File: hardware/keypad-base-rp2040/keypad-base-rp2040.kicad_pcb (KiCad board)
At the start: 2 copper layers, 150.2 x 64.2 mm, 66 parts, among them CON1 AVR-ISP-6, J1 USB_C_Receptacle_USB2.0, J2 Conn_01x02, J3 Conn_01x02, Q1 AO3400A, SW1 Switch_SW_Push, SW2 Switch_SW_Push, SW3 Switch_SW_Push, SW4 Switch_SW_Push, SW5 Switch_SW_Push, SW6 Switch_SW_Push, SW7 Switch_SW_Push, SW8 Switch_SW_Push, U1 ATmega32U4-MU, U10 AP2112K-3.3, U11 W25Q128JVS, U3 IE096HQ1301CL, U4 IE096HQ1301CL, U5 IE096HQ1301CL, U6 IE096HQ1301CL, U7 IE096HQ1301CL, U8 IE096HQ1301CL, X1 16MHz

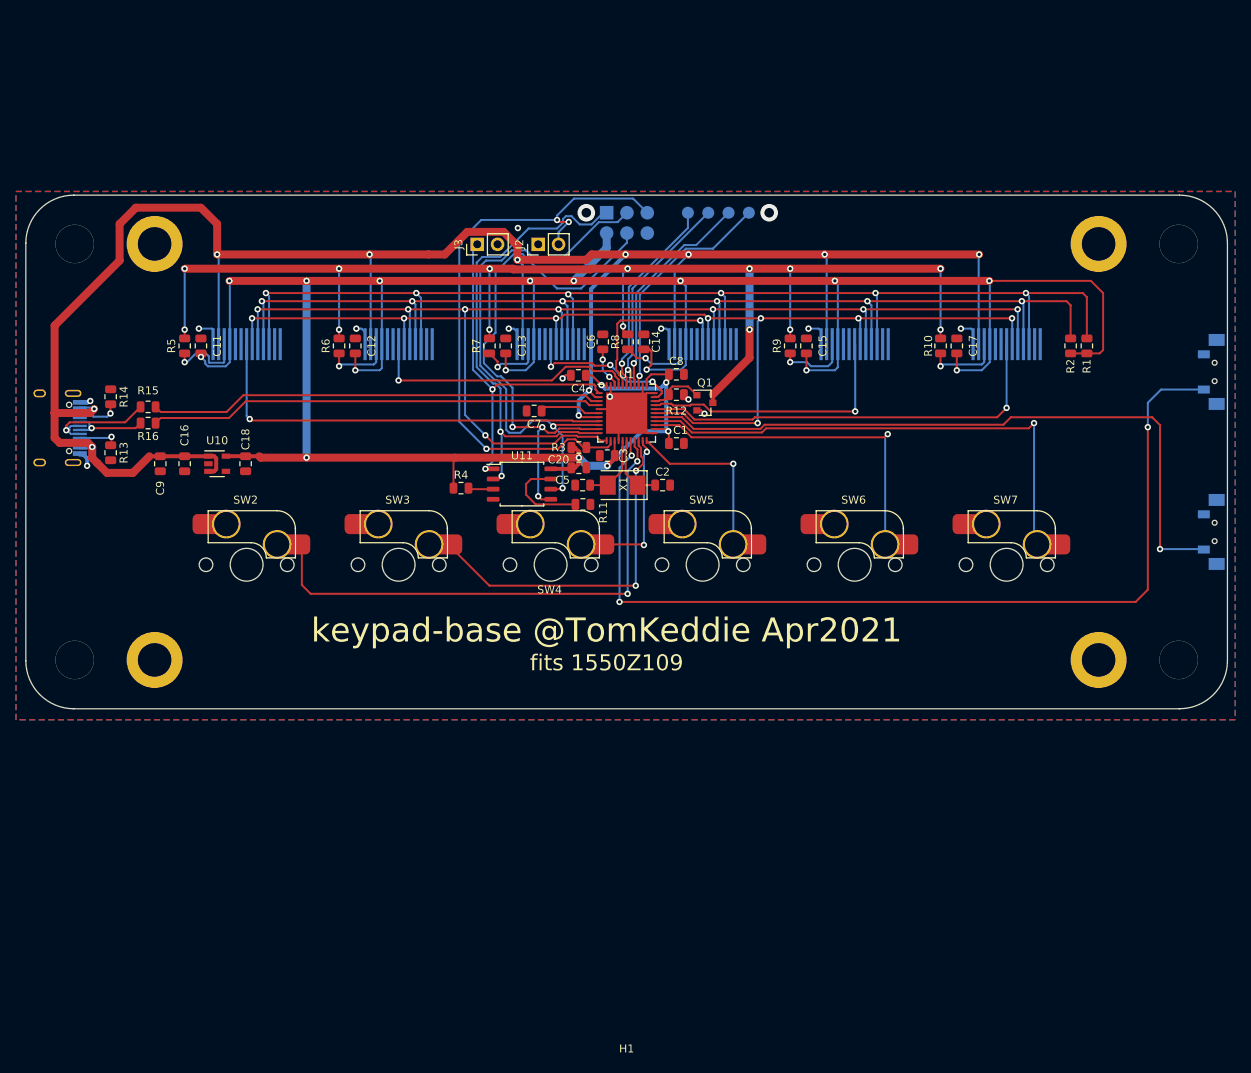
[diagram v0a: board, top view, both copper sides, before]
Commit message: hardware/keypad-base-rp2040: update to latest kicad file format
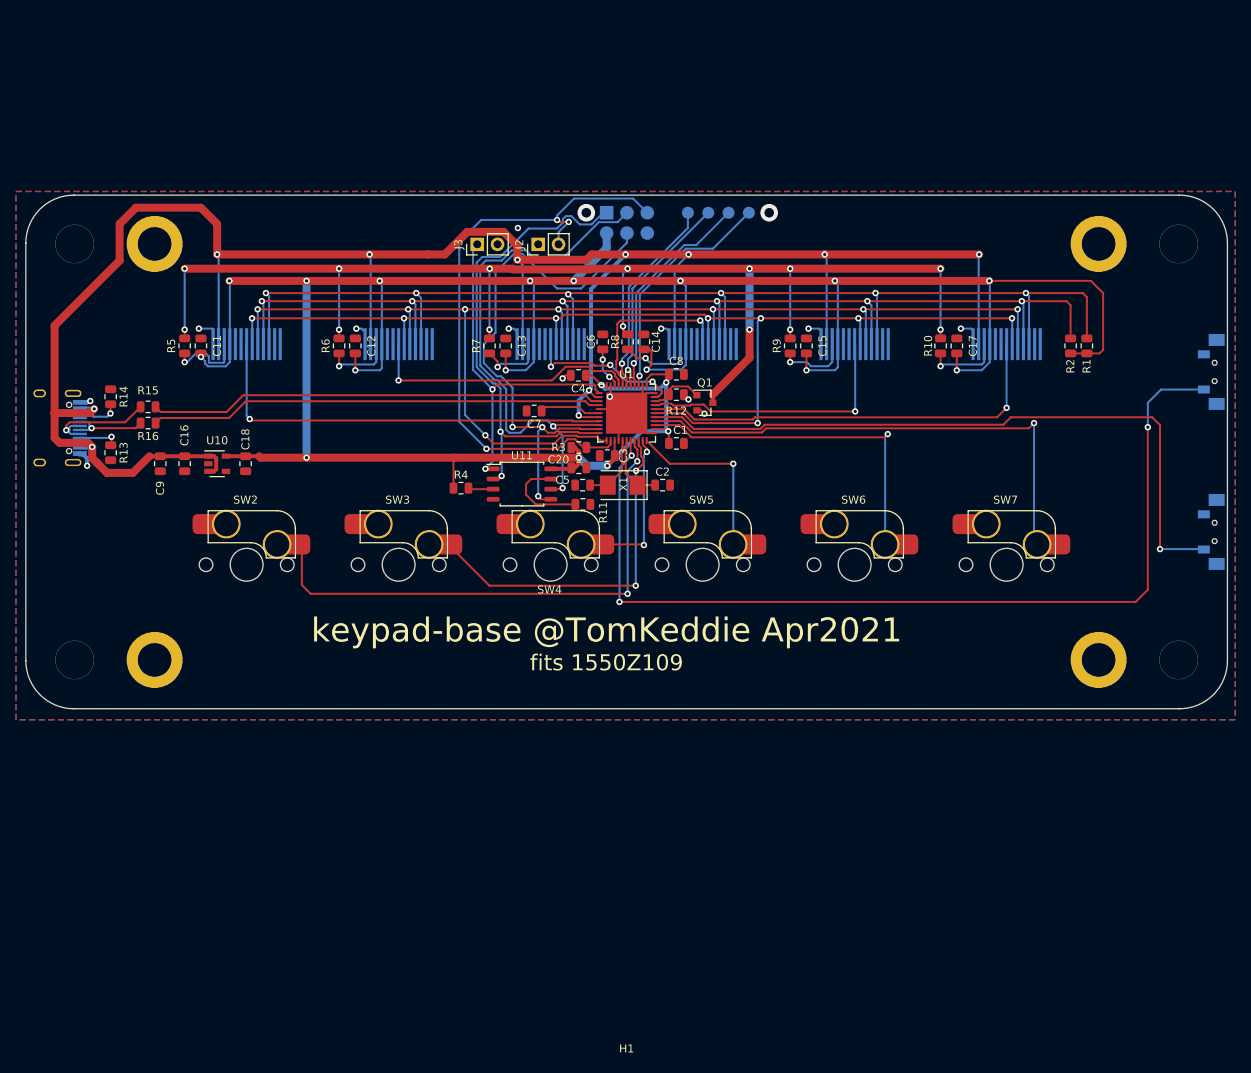
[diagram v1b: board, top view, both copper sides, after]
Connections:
- net /~CS2 renamed /~{CS2}
- net /~CS3 renamed /~{CS3}
- net /~CS4 renamed /~{CS4}
- net /~CS5 renamed /~{CS5}
- net /~CS6 renamed /~{CS6}
- net /~CS7 renamed /~{CS7}
- net /~FLASH_CS renamed /~{FLASH_CS}
- net /~LCDRESET renamed /~{LCDRESET}
- net /~RESET renamed /~{RESET}
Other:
- net class Default removed

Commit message: hardware/keypad0base-rp2040: first pass at rp2040 based design
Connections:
- U1 pad 29: /~{CS7} -> /~{CS6}
- U1 pad 30: /~{CS6} -> /~{CS5}
- U1 pad 32: /~{CS5} -> /~{CS4}
- U1 pad 40: /~{CS4} -> /~{CS3}
- U1 pad 41: /~{CS3} -> /~{CS2}
- U1 pad 8: /~{CS2} -> /~{CS1}
- U3 pad 7: /~{CS2} -> /~{CS1}
- U4 pad 7: /~{CS3} -> /~{CS2}
- U5 pad 7: /~{CS5} -> /~{CS4}
- U6 pad 7: /~{CS4} -> /~{CS3}
- U7 pad 7: /~{CS6} -> /~{CS5}
- U8 pad 7: /~{CS7} -> /~{CS6}
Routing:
- net /~{CS1}: track 0.00 -> 53.3 mm, vias 0 -> 1
- net /~{CS7}: track 53.2 -> 0.00 mm, vias 1 -> 0
- net /~{CS6}: track 34.1 -> 53.2 mm
- net /~{CS2}: track 53.3 -> 34.3 mm
- net /~{CS5}: track 19.8 -> 34.1 mm, vias 3 -> 1
- net /~{CS3}: track 34.3 -> 21.7 mm
- net /~{CS4}: track 21.7 -> 19.8 mm, vias 1 -> 3
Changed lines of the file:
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@@
   (net 36 "Net-(U3-Pad1)")
   (net 37 "Net-(U3-Pad2)")
-  (net 38 "/~{CS2}")
+  (net 38 "/~{CS1}")
   (net 39 "Net-(U4-Pad1)")
   (net 40 "Net-(U4-Pad2)")
-  (net 41 "/~{CS3}")
+  (net 41 "/~{CS2}")
   (net 42 "Net-(U5-Pad1)")
   (net 43 "Net-(U5-Pad2)")
-  (net 44 "/~{CS5}")
+  (net 44 "/~{CS4}")
   (net 45 "Net-(U6-Pad1)")
   (net 46 "Net-(U6-Pad2)")
-  (net 47 "/~{CS4}")
+  (net 47 "/~{CS3}")
   (net 48 "Net-(U7-Pad1)")
   (net 49 "Net-(U7-Pad2)")
-  (net 50 "/~{CS6}")
+  (net 50 "/~{CS5}")
   (net 51 "Net-(U8-Pad1)")
   (net 52 "Net-(U8-Pad2)")
-  (net 53 "/~{CS7}")
+  (net 53 "/~{CS6}")
   (net 54 "/USB_N")
   (net 55 "/USB_P")
@@
       (net 24 "+5V"))
     (pad "8" smd roundrect locked (at -3.4375 1) (size 0.875 0.25) (layers "F.Cu" "F.Paste" "F.Mask") (roundrect_rratio 0.25)
-      (net 38 "/~{CS2}"))
+      (net 38 "/~{CS1}"))
     (pad "9" smd roundrect locked (at -3.4375 1.5) (size 0.875 0.25) (layers "F.Cu" "F.Paste" "F.Mask") (roundrect_rratio 0.25)
       (net 8 "/SCK"))
@@
       (net 26 "/~{LCDRESET}"))
     (pad "29" smd roundrect locked (at 3.4375 -0.5) (size 0.875 0.25) (layers "F.Cu" "F.Paste" "F.Mask") (roundrect_rratio 0.25)
-      (net 53 "/~{CS7}"))
+      (net 53 "/~{CS6}"))
     (pad "30" smd roundrect locked (at 3.4375 -1) (size 0.875 0.25) (layers "F.Cu" "F.Paste" "F.Mask") (roundrect_rratio 0.25)
-      (net 50 "/~{CS6}"))
+      (net 50 "/~{CS5}"))
     (pad "31" smd roundrect locked (at 3.4375 -1.5) (size 0.875 0.25) (layers "F.Cu" "F.Paste" "F.Mask") (roundrect_rratio 0.25)
       (net 29 "/BACKLIGHT"))
     (pad "32" smd roundrect locked (at 3.4375 -2) (size 0.875 0.25) (layers "F.Cu" "F.Paste" "F.Mask") (roundrect_rratio 0.25)
-      (net 44 "/~{CS5}"))
+      (net 44 "/~{CS4}"))
     (pad "33" smd roundrect locked (at 3.4375 -2.5) (size 0.875 0.25) (layers "F.Cu" "F.Paste" "F.Mask") (roundrect_rratio 0.25)
       (net 1 "GND"))
@@
       (net 20 "/TCK"))
     (pad "40" smd roundrect locked (at -0.5 -3.4375) (size 0.25 0.875) (layers "F.Cu" "F.Paste" "F.Mask") (roundrect_rratio 0.25)
-      (net 47 "/~{CS4}"))
+      (net 47 "/~{CS3}"))
     (pad "41" smd roundrect locked (at -1 -3.4375) (size 0.25 0.875) (layers "F.Cu" "F.Paste" "F.Mask") (roundrect_rratio 0.25)
-      (net 41 "/~{CS3}"))
+      (net 41 "/~{CS2}"))
     (pad "42" smd roundrect locked (at -1.5 -3.4375) (size 0.25 0.875) (layers "F.Cu" "F.Paste" "F.Mask") (roundrect_rratio 0.25)
       (net 5 "/AREF"))
@@
       (net 26 "/~{LCDRESET}"))
     (pad "7" smd rect locked (at 0 0 180) (size 0.4 4) (layers "B.Cu" "B.Paste" "B.Mask")
-      (net 38 "/~{CS2}"))
+      (net 38 "/~{CS1}"))
     (pad "8" smd rect locked (at 0.7 0 180) (size 0.4 4) (layers "B.Cu" "B.Paste" "B.Mask")
       (net 1 "GND"))
@@
       (net 26 "/~{LCDRESET}"))
     (pad "7" smd rect locked (at 0 0 180) (size 0.4 4) (layers "B.Cu" "B.Paste" "B.Mask")
-      (net 41 "/~{CS3}"))
+      (net 41 "/~{CS2}"))
     (pad "8" smd rect locked (at 0.7 0 180) (size 0.4 4) (layers "B.Cu" "B.Paste" "B.Mask")
       (net 1 "GND"))
@@
       (net 26 "/~{LCDRESET}"))
     (pad "7" smd rect locked (at 0 0 180) (size 0.4 4) (layers "B.Cu" "B.Paste" "B.Mask")
-      (net 47 "/~{CS4}"))
+      (net 47 "/~{CS3}"))
     (pad "8" smd rect locked (at 0.7 0 180) (size 0.4 4) (layers "B.Cu" "B.Paste" "B.Mask")
       (net 1 "GND"))
@@
       (net 26 "/~{LCDRESET}"))
     (pad "7" smd rect locked (at 0 0 180) (size 0.4 4) (layers "B.Cu" "B.Paste" "B.Mask")
-      (net 50 "/~{CS6}"))
+      (net 50 "/~{CS5}"))
     (pad "8" smd rect locked (at 0.7 0 180) (size 0.4 4) (layers "B.Cu" "B.Paste" "B.Mask")
       (net 1 "GND"))
@@
       (net 26 "/~{LCDRESET}"))
     (pad "7" smd rect locked (at 0 0 180) (size 0.4 4) (layers "B.Cu" "B.Paste" "B.Mask")
-      (net 53 "/~{CS7}"))
+      (net 53 "/~{CS6}"))
     (pad "8" smd rect locked (at 0.7 0 180) (size 0.4 4) (layers "B.Cu" "B.Paste" "B.Mask")
       (net 1 "GND"))
@@
       (net 26 "/~{LCDRESET}"))
     (pad "7" smd rect locked (at 0 0 180) (size 0.4 4) (layers "B.Cu" "B.Paste" "B.Mask")
-      (net 44 "/~{CS5}"))
+      (net 44 "/~{CS4}"))
     (pad "8" smd rect locked (at 0.7 0 180) (size 0.4 4) (layers "B.Cu" "B.Paste" "B.Mask")
       (net 1 "GND"))

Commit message: hardware/keypad-base-rp2040: progress commit
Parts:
- removed CON1: AVR-ISP-6, tom-connectors:PinTestpoint_2x03_P2.54mm_Vertical
- removed J2: Conn_01x02, tom-connectors:PinHeader_1x02_P2.54mm_Vertical
- removed R16: 22R, tom-passives:R_0805_2012Metric
- removed TCK1: TCK, tom-mechanical:TestPoint_Pad_D1.5mm
- removed TDI1: TDI, tom-mechanical:TestPoint_Pad_D1.5mm
- removed TDO1: TDO, tom-mechanical:TestPoint_Pad_D1.5mm
- removed TMS1: TMS, tom-mechanical:TestPoint_Pad_D1.5mm
- added C10: 100nF,16V,X7R, tom-passives:C_0402_1005Metric, F.Cu at (153.7, 39.6)
- added C19: 10uF,6.3V,X5R, tom-passives:C_0402_1005Metric, F.Cu at (151.4, 72.4)
- added C21: 10uF,6.3V,X5R, tom-passives:C_0402_1005Metric, F.Cu at (189.0, 72.4)
- added C22: 10uF,6.3V,X5R, tom-passives:C_0402_1005Metric, F.Cu at (207.8, 72.4)
- added SW9: Switch_SW_Push, tom-mechanical:SW_SPST_SMD_SIDE_C319395, B.Cu at (120.9, 55.4)
- C1: value 0.1uF/6.3V -> 20pF,50V,C0G; footprint tom-passives:C_0805_2012Metric -> tom-passives:C_0402_1005Metric
- C11, C12, C13, C14, C3, C4, C6, C8: value 0.1uF/6.3V -> 100nF,16V,X7R; footprint tom-passives:C_0805_2012Metric -> tom-passives:C_0402_1005Metric
- C15, C17, C20: value 0.1uF/6.3V -> 10uF,6.3V,X5R; footprint tom-passives:C_0805_2012Metric -> tom-passives:C_0402_1005Metric
- C16, C18: value 1uF/6.3V -> 1uF,25V,X5R; footprint tom-passives:C_0805_2012Metric -> tom-passives:C_0402_1005Metric
- C2: value 18pF -> 20pF,50V,C0G; footprint tom-passives:C_0805_2012Metric -> tom-passives:C_0402_1005Metric
- C5: value 18pF -> 10uF,6.3V,X5R; footprint tom-passives:C_0805_2012Metric -> tom-passives:C_0402_1005Metric
- C7: value 1uF/6.3V -> 100nF,16V,X7R; footprint tom-passives:C_0805_2012Metric -> tom-passives:C_0402_1005Metric
- C9: value 10uF/10V -> 10uF,10V,X5R; footprint tom-passives:C_0805_2012Metric -> tom-passives:C_0603_1608Metric
- J3: value Conn_01x02 -> Conn_02x05_SWD; footprint tom-connectors:PinHeader_1x02_P2.54mm_Vertical -> tom-connectors:FTSH-105-01-F-DV-K
- R1: value 10k -> 1k; footprint tom-passives:R_0805_2012Metric -> tom-passives:R_0402_1005Metric
- R10, R6, R9: value 470R -> 470; footprint tom-passives:R_0805_2012Metric -> tom-passives:R_0402_1005Metric
- R11, R12: value 10k -> 470; footprint tom-passives:R_0805_2012Metric -> tom-passives:R_0402_1005Metric
- R13: value 5.1k -> 470; footprint tom-passives:R_0805_2012Metric -> tom-passives:R_0402_1005Metric
- R14: value 5.1k -> 1k; footprint tom-passives:R_0805_2012Metric -> tom-passives:R_0402_1005Metric
- R15: value 22R -> 10k; footprint tom-passives:R_0805_2012Metric -> tom-passives:R_0402_1005Metric
- R2: value 10k -> 5.1k; footprint tom-passives:R_0805_2012Metric -> tom-passives:R_0402_1005Metric
- R3, R4: value 10k -> 27; footprint tom-passives:R_0805_2012Metric -> tom-passives:R_0603_1608Metric
- R5: value 470R -> 5.1k; footprint tom-passives:R_0805_2012Metric -> tom-passives:R_0402_1005Metric
- R7, R8: value 470R -> 10k; footprint tom-passives:R_0805_2012Metric -> tom-passives:R_0402_1005Metric
- SW7: renamed from SW8; footprint tom-mechanical:SW_SPST_SMD_SIDE_7.0x3.5 -> tom-mechanical:SW_SPST_SMD_SIDE_C319395
- SW8: renamed from SW1; footprint tom-mechanical:SW_SPST_SMD_SIDE_7.0x3.5 -> tom-mechanical:SW_SPST_SMD_SIDE_C319395
- U1: value ATmega32U4-MU -> RP2040; footprint tom-semiconductors:QFN-44-1EP_7x7mm_P0.5mm_EP5.15x5.15mm -> tom-semiconductors:RP2040-QFN-56
- X1: value 16MHz -> 12MHz; footprint tom-passives:Crystal_SMD_5032-2Pin_5.0x3.2mm -> tom-passives:Crystal_SMD_3225-4Pin_3.2x2.5mm
- moved R2 120.0 mm to (102.6, 85.1), turned to 0 degrees
- moved R13 104.6 mm to (205.7, 72.4), turned to 90 degrees
- moved J3 78.8 mm to (175.3, 133.9), turned to 0 degrees
- moved C15 75.7 mm to (113.3, 72.1)
- moved C17 75.2 mm to (132.6, 72.4)
- moved R15 62.4 mm to (150.8, 36.1), turned to 0 degrees
- moved C16 61.4 mm to (147.8, 38.1), turned to 0 degrees
- moved C18 58.7 mm to (150.8, 38.1), turned to 0 degrees
- moved C11 57.0 mm to (156.6, 35.6), turned to 0 degrees
- moved R10 56.4 mm to (149.4, 72.4)
- moved R9 56.4 mm to (130.6, 72.4)
- moved C9 54.7 mm to (140.1, 43.0), turned to 0 degrees
- moved R3 54.1 mm to (106.7, 80.0), turned to 180 degrees
- moved C3 53.3 mm to (156.6, 33.6), turned to 0 degrees
- moved C5 50.7 mm to (156.6, 39.6), turned to 0 degrees
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- renumbered SW2 to SW1, SW3 to SW2, SW4 to SW3, SW5 to SW4, SW6 to SW5, SW7 to SW6, U6 to U5, U5 to U6
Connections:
- C1 pad 1: +3V3 -> /XIN
- C11 pad 1: +3V3 -> +3.3V
- C12 pad 1: +3V3 -> +3.3V
- C13 pad 1: +3V3 -> +3.3V
- C14 pad 1: +3V3 -> +3.3V
- C15 pad 1: +3V3 -> +3.3V
- C17 pad 1: +3V3 -> +3.3V
- C18 pad 1: +3V3 -> +3.3V
- C2 pad 1: /XTAL1 -> Net-(C2-Pad1)
- C20 pad 1: +3V3 -> +3.3V
- C3 pad 1: +3V3 -> +1V1
- C4 pad 1: +3V3 -> +1V1
- C5 pad 1: /XTAL2 -> +1V1
- C6 pad 1: GND -> +3.3V
- C6 pad 2: /AREF -> GND
- C7 pad 1: /UCAP -> +3.3V
- C8 pad 1: +3V3 -> +3.3V
- J1 pad A8: Net-(J1-PadA8) -> unconnected-(J1-PadA8)
- J1 pad B8: Net-(J1-PadB8) -> unconnected-(J1-PadB8)
- J3 pad 1: /~{FLASH_CS} -> +3.3V
- J3 pad 2: GND -> /SWD
- R1 pad 1: +3V3 -> /XOUT
- R1 pad 2: /SDA -> Net-(C2-Pad1)
- R10 pad 1: Net-(R10-Pad1) -> Net-(U5-Pad11)
- R11 pad 1: GND -> Net-(U6-Pad11)
- R11 pad 2: Net-(R11-Pad2) -> /BACKLIGHTK
- R12 pad 1: /BACKLIGHT -> Net-(U7-Pad11)
- R12 pad 2: GND -> /BACKLIGHTK
- R13 pad 1: /CC1 -> Net-(U8-Pad11)
- R13 pad 2: GND -> /BACKLIGHTK
- R14 pad 1: GND -> /QSPI_SS
- R14 pad 2: /CC2 -> /BOOTSEL
- R15 pad 1: /USB_N -> /BACKLIGHT
- R15 pad 2: /D_N -> GND
- R2 pad 1: +3V3 -> /CC1
- R2 pad 2: /SCL -> GND
- R3 pad 1: +3V3 -> /USB_N
- R3 pad 2: /~{RESET} -> /D_N
- R4 pad 1: +3V3 -> /USB_P
- R4 pad 2: Net-(R4-Pad2) -> /D_P
- R5 pad 1: Net-(R5-Pad1) -> /CC2
- R5 pad 2: /BACKLIGHTK -> GND
- R6 pad 1: Net-(R6-Pad1) -> Net-(U3-Pad11)
- R7 pad 1: Net-(R7-Pad1) -> +3.3V
- R7 pad 2: /BACKLIGHTK -> /~{RESET}
- R8 pad 1: Net-(R8-Pad1) -> +3.3V
- R8 pad 2: /BACKLIGHTK -> /QSPI_SS
- R9 pad 1: Net-(R9-Pad1) -> Net-(U4-Pad11)
- SW1 pad 2: /SW2 -> /SW1
- SW2 pad 2: /SW3 -> /SW2
- SW3 pad 2: /SW4 -> /SW3
- SW4 pad 2: /SW5 -> /SW4
- SW5 pad 2: /SW6 -> /SW5
- SW6 pad 2: /SW7 -> /SW6
- SW7 pad 2: /SW8 -> /SW7
- SW8 pad 2: /SW1 -> /SW8
- U1 pad 1: /~{FLASH_CS} -> +3.3V
- U1 pad 10: /MOSI -> +3.3V
- U1 pad 11: /MISO -> /SW1
- U1 pad 12: /D\C -> /SW2
- U1 pad 13: /~{RESET} -> /SW3
- U1 pad 14: +3V3 -> /SW4
- U1 pad 15: GND -> /SW5
- U1 pad 16: /XTAL2 -> /SW6
- U1 pad 17: /XTAL1 -> /SW7
- U1 pad 18: /SW1 -> /SW8
- U1 pad 19: /SW2 -> GND
- U1 pad 2: +5V -> unconnected-(U1-Pad2)
- U1 pad 20: /SW3 -> /XIN
- U1 pad 21: /SW4 -> /XOUT
- U1 pad 22: /SW5 -> +3.3V
- U1 pad 23: GND -> +1V1
- U1 pad 24: +3V3 -> /SWCLK
- U1 pad 25: /SW6 -> /SWD
- U1 pad 26: /SW7 -> /~{RESET}
- U1 pad 27: /SW8 -> unconnected-(U1-Pad27)
- U1 pad 28: /~{LCDRESET} -> unconnected-(U1-Pad28)
- U1 pad 29: /~{CS6} -> unconnected-(U1-Pad29)
- U1 pad 3: /USB_N -> unconnected-(U1-Pad3)
- U1 pad 30: /~{CS5} -> unconnected-(U1-Pad30)
- U1 pad 31: /BACKLIGHT -> /~{LCDRESET}
- U1 pad 32: /~{CS4} -> /BACKLIGHT
- U1 pad 33: GND -> +3.3V
- U1 pad 34: +3V3 -> /D\C
- U1 pad 35: GND -> /~{CS6}
- U1 pad 36: /TDI -> /~{CS5}
- U1 pad 37: /TDO -> unconnected-(U1-Pad37)
- U1 pad 38: /TMS -> /~{CS4}
- U1 pad 39: /TCK -> /~{CS3}
- U1 pad 4: /USB_P -> /SCLK
- U1 pad 40: /~{CS3} -> /~{CS2}
- U1 pad 41: /~{CS2} -> /~{CS1}
- U1 pad 42: /AREF -> +3.3V
- U1 pad 43: GND -> unconnected-(U1-Pad43)
- U1 pad 44: +3V3 -> +3.3V
- U1 pad 45: GND -> +1V1
- U1 pad 5: GND -> /MOSI
- U1 pad 6: /UCAP -> unconnected-(U1-Pad6)
- U1 pad 7: +5V -> unconnected-(U1-Pad7)
- U1 pad 8: /~{CS1} -> unconnected-(U1-Pad8)
- U1 pad 9: /SCK -> unconnected-(U1-Pad9)
- U10 pad 4: Net-(U10-Pad4) -> unconnected-(U10-Pad4)
- U10 pad 5: +3V3 -> +3.3V
- U11 pad 1: /~{FLASH_CS} -> /QSPI_SS
- U11 pad 2: /MISO -> /QSPI_SD1
- U11 pad 3: Net-(R4-Pad2) -> /QSPI_SD2
- U11 pad 5: /MOSI -> /QSPI_SD0
- U11 pad 6: /SCK -> /QSPI_SCLK
- U11 pad 7: Net-(R11-Pad2) -> /QSPI_SD3
- U11 pad 8: +3V3 -> +3.3V
- U3 pad 1: Net-(U3-Pad1) -> unconnected-(U3-Pad1)
- U3 pad 10: +3V3 -> +3.3V
- U3 pad 11: Net-(R5-Pad1) -> Net-(U3-Pad11)
- U3 pad 2: Net-(U3-Pad2) -> unconnected-(U3-Pad2)
- U3 pad 3: /SDA -> /MOSI
- U3 pad 4: /SCL -> /SCLK
- U4 pad 1: Net-(U4-Pad1) -> unconnected-(U4-Pad1)
- U4 pad 10: +3V3 -> +3.3V
- U4 pad 11: Net-(R6-Pad1) -> Net-(U4-Pad11)
- U4 pad 2: Net-(U4-Pad2) -> unconnected-(U4-Pad2)
- U4 pad 3: /SDA -> /MOSI
- U4 pad 4: /SCL -> /SCLK
- U5 pad 1: Net-(U6-Pad1) -> unconnected-(U5-Pad1)
- U5 pad 10: +3V3 -> +3.3V
- U5 pad 11: Net-(R8-Pad1) -> Net-(U5-Pad11)
- U5 pad 2: Net-(U6-Pad2) -> unconnected-(U5-Pad2)
- U5 pad 3: /SDA -> /MOSI
- U5 pad 4: /SCL -> /SCLK
- U6 pad 1: Net-(U5-Pad1) -> unconnected-(U6-Pad1)
- U6 pad 10: +3V3 -> +3.3V
- U6 pad 11: Net-(R7-Pad1) -> Net-(U6-Pad11)
- U6 pad 2: Net-(U5-Pad2) -> unconnected-(U6-Pad2)
- U6 pad 3: /SDA -> /MOSI
- U6 pad 4: /SCL -> /SCLK
- U7 pad 1: Net-(U7-Pad1) -> unconnected-(U7-Pad1)
- U7 pad 10: +3V3 -> +3.3V
- U7 pad 11: Net-(R9-Pad1) -> Net-(U7-Pad11)
- U7 pad 2: Net-(U7-Pad2) -> unconnected-(U7-Pad2)
- U7 pad 3: /SDA -> /MOSI
- U7 pad 4: /SCL -> /SCLK
- U8 pad 1: Net-(U8-Pad1) -> unconnected-(U8-Pad1)
- U8 pad 10: +3V3 -> +3.3V
- U8 pad 11: Net-(R10-Pad1) -> Net-(U8-Pad11)
- U8 pad 2: Net-(U8-Pad2) -> unconnected-(U8-Pad2)
- U8 pad 3: /SDA -> /MOSI
- U8 pad 4: /SCL -> /SCLK
- X1 pad 1: /XTAL1 -> /XIN
- X1 pad 2: /XTAL2 -> GND
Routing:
- net +3V3: track 350.4 -> 0.00 mm, vias 20 -> 0
- net +3.3V: track 0.00 -> 222.8 mm, vias 0 -> 14
- net /SDA: track 147.4 -> 0.00 mm, vias 6 -> 0
- net /SCL: track 138.6 -> 0.00 mm, vias 6 -> 0
- net /SCLK: track 0.00 -> 128.1 mm, vias 0 -> 6
- net /SW1: track 118.6 -> 2.39 mm, vias 3 -> 0
- net /SW8: track 85.9 -> 0.00 mm, vias 1 -> 0
- net /~{RESET}: track 76.1 -> 0.00 mm, vias 3 -> 0
- net /MOSI: track 66.4 -> 134.4 mm, vias 3 -> 6
- net /SCK: track 66.7 -> 0.00 mm, vias 2 -> 0
- net /SW7: track 66.3 -> 0.00 mm, vias 1 -> 0
- net /SW2: track 68.4 -> 2.39 mm, vias 2 -> 0
- net /MISO: track 62.1 -> 0.00 mm, vias 2 -> 0
- net /USB_P: track 56.8 -> 0.00 mm
- net /USB_N: track 56.9 -> 0.91 mm
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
